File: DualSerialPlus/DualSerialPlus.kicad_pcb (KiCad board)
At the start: 2 copper layers, 99.8 x 99 mm, 22 parts, among them CN1 DB9 Male, CN2 DB9 Male, J1 COM_A_SELECT, J2 IRQ_A_SELECT, J3 COM_A_SELECT, J4 IRQ_B_SELECT, J5 Input BUS, U1 16550/16C550, U2 GAL16V8, U3 GD75232N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

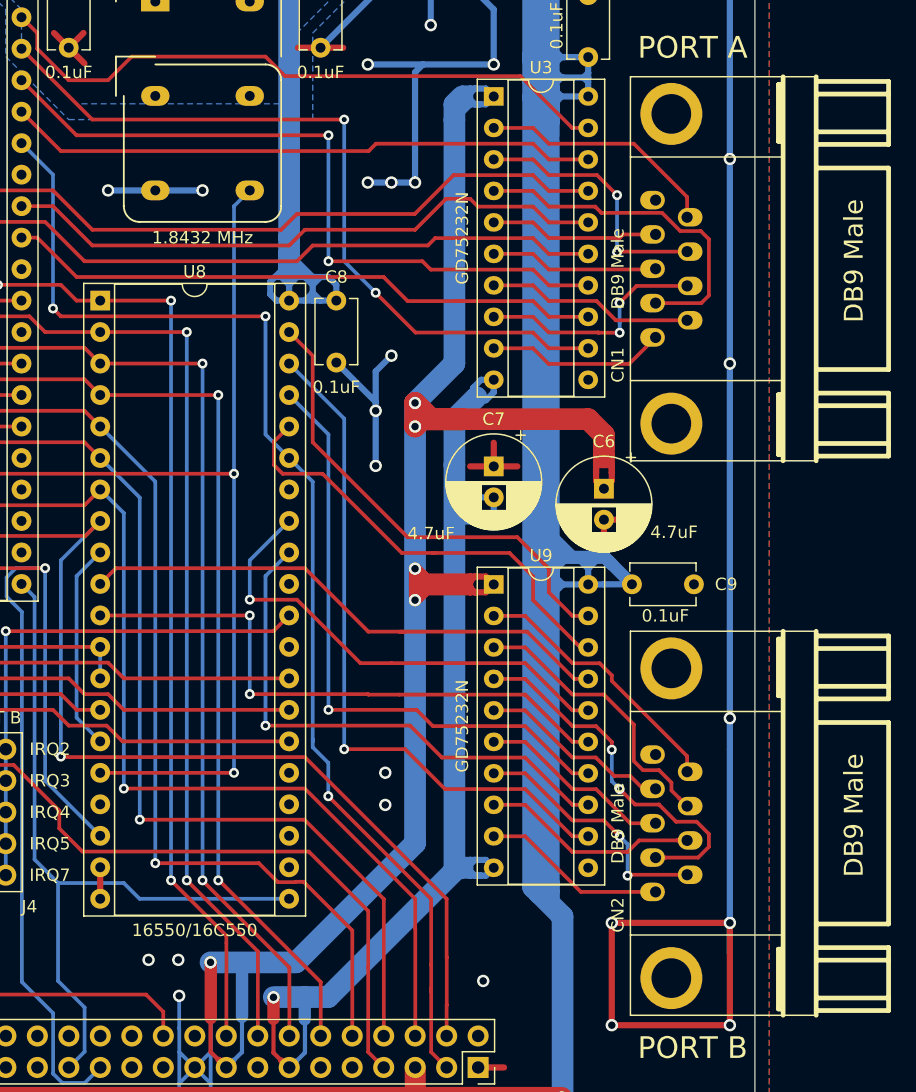
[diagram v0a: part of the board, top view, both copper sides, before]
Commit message: Realized on PLUS cards, the ports need to be on the UNDERSIDE to line up properly
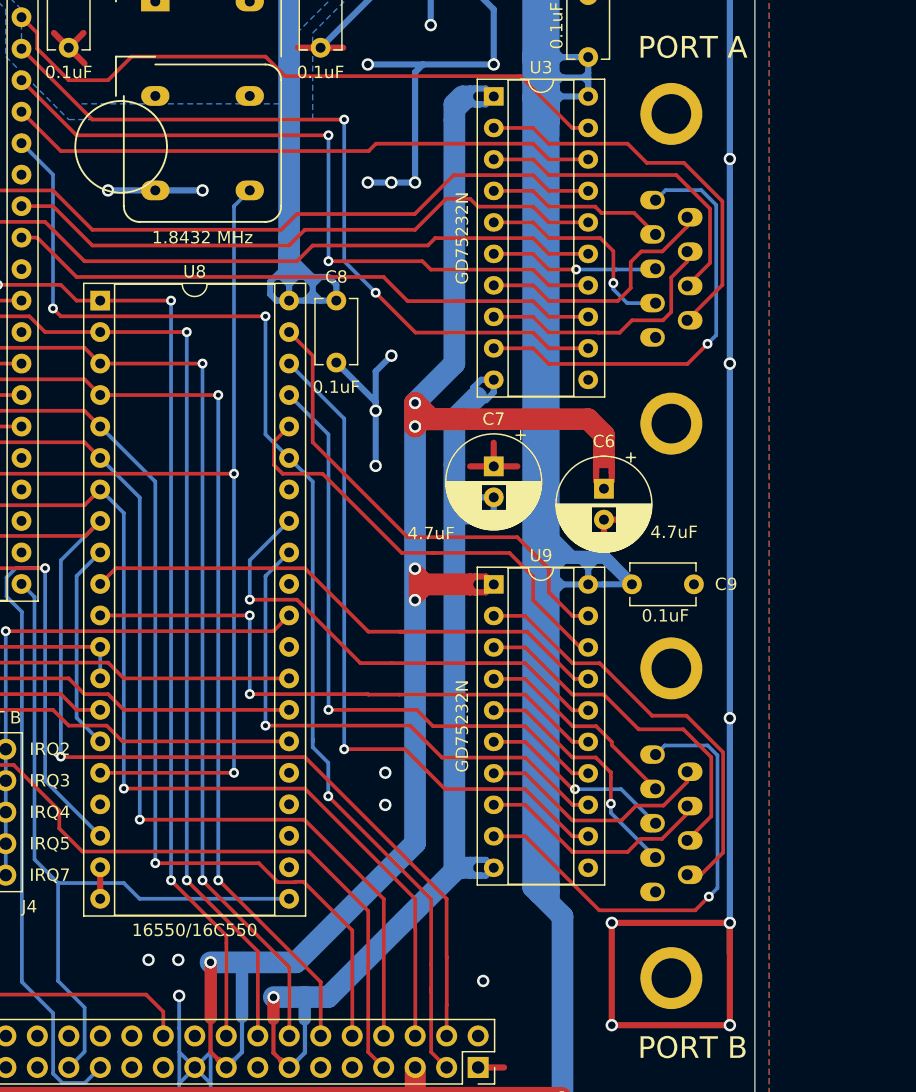
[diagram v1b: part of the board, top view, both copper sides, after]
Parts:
- CN1, CN2: moved to B.Cu
- turned CN1 to -90 degrees
- turned CN2 to -90 degrees
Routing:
- net /SERB_PIN1: track 14.9 -> 37.6 mm, vias 0 -> 1
- net /SERA_PIN1: track 14.5 -> 35.7 mm, vias 0 -> 1
- net /SERB_PIN2: track 30.9 -> 16.9 mm, vias 2 -> 0
- net /SERA_PIN2: track 28.1 -> 14.5 mm
- net /SERB_PIN9: track 21.8 -> 34.8 mm
- net /SERA_PIN9: track 19.5 -> 31.7 mm
- net /SERB_PIN8: track 23.9 -> 28.7 mm
- net /SERA_PIN8: track 21.4 -> 26.1 mm, vias 2 -> 0
- net /SERA_PIN6: track 16.8 -> 21.2 mm
- net /SERA_PIN4: track 13.7 -> 17.6 mm, vias 0 -> 1
- net /SERB_PIN4: track 16.2 -> 19.9 mm, vias 0 -> 1
- net /SERA_PIN7: track 19.1 -> 20.9 mm, vias 2 -> 0
- net /SERB_PIN6: track 20.5 -> 19.3 mm, vias 2 -> 0
- net /SERB_PIN7: track 18.4 -> 19.1 mm
- net /SERA_PIN3: track 13.6 -> 13.7 mm, vias 0 -> 1
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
